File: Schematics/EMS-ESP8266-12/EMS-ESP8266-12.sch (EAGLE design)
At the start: 45 parts, among them IC1 LM393N, J99 Upload, T1 BC547B, T2 BC547B

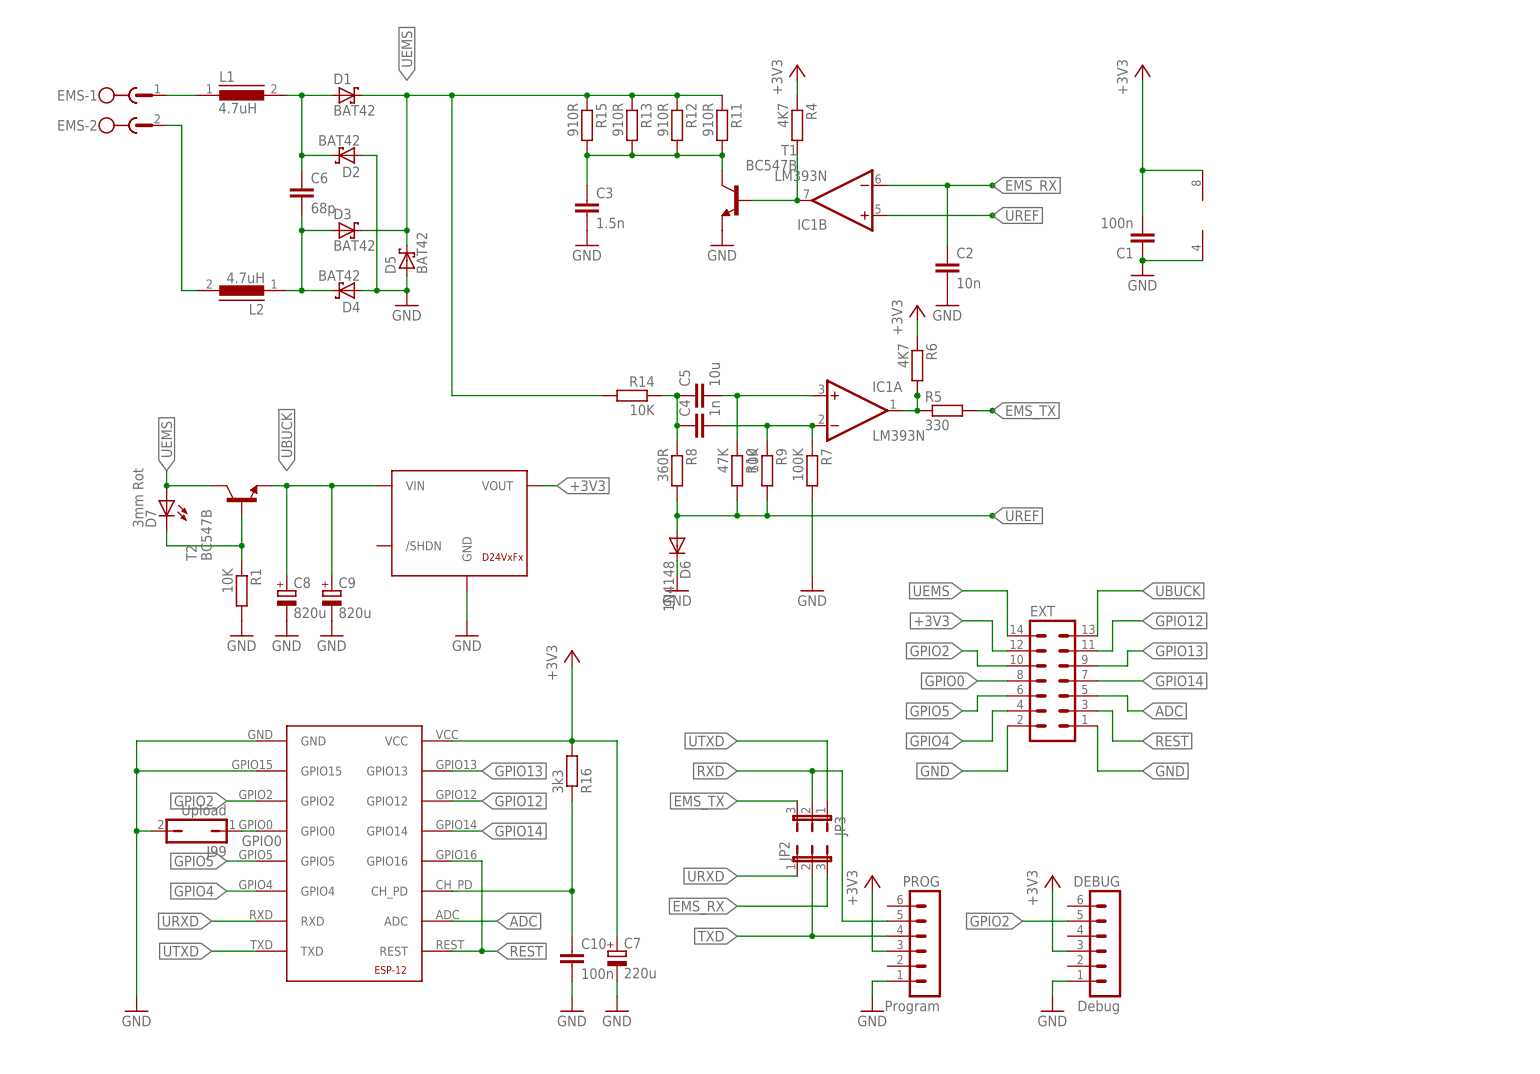
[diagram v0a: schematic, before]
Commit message: PCB reworked ° remove ground layer below ESP12-antenna ° change connector footprint ° 2pin debug connector ° small form factor for EMS connector
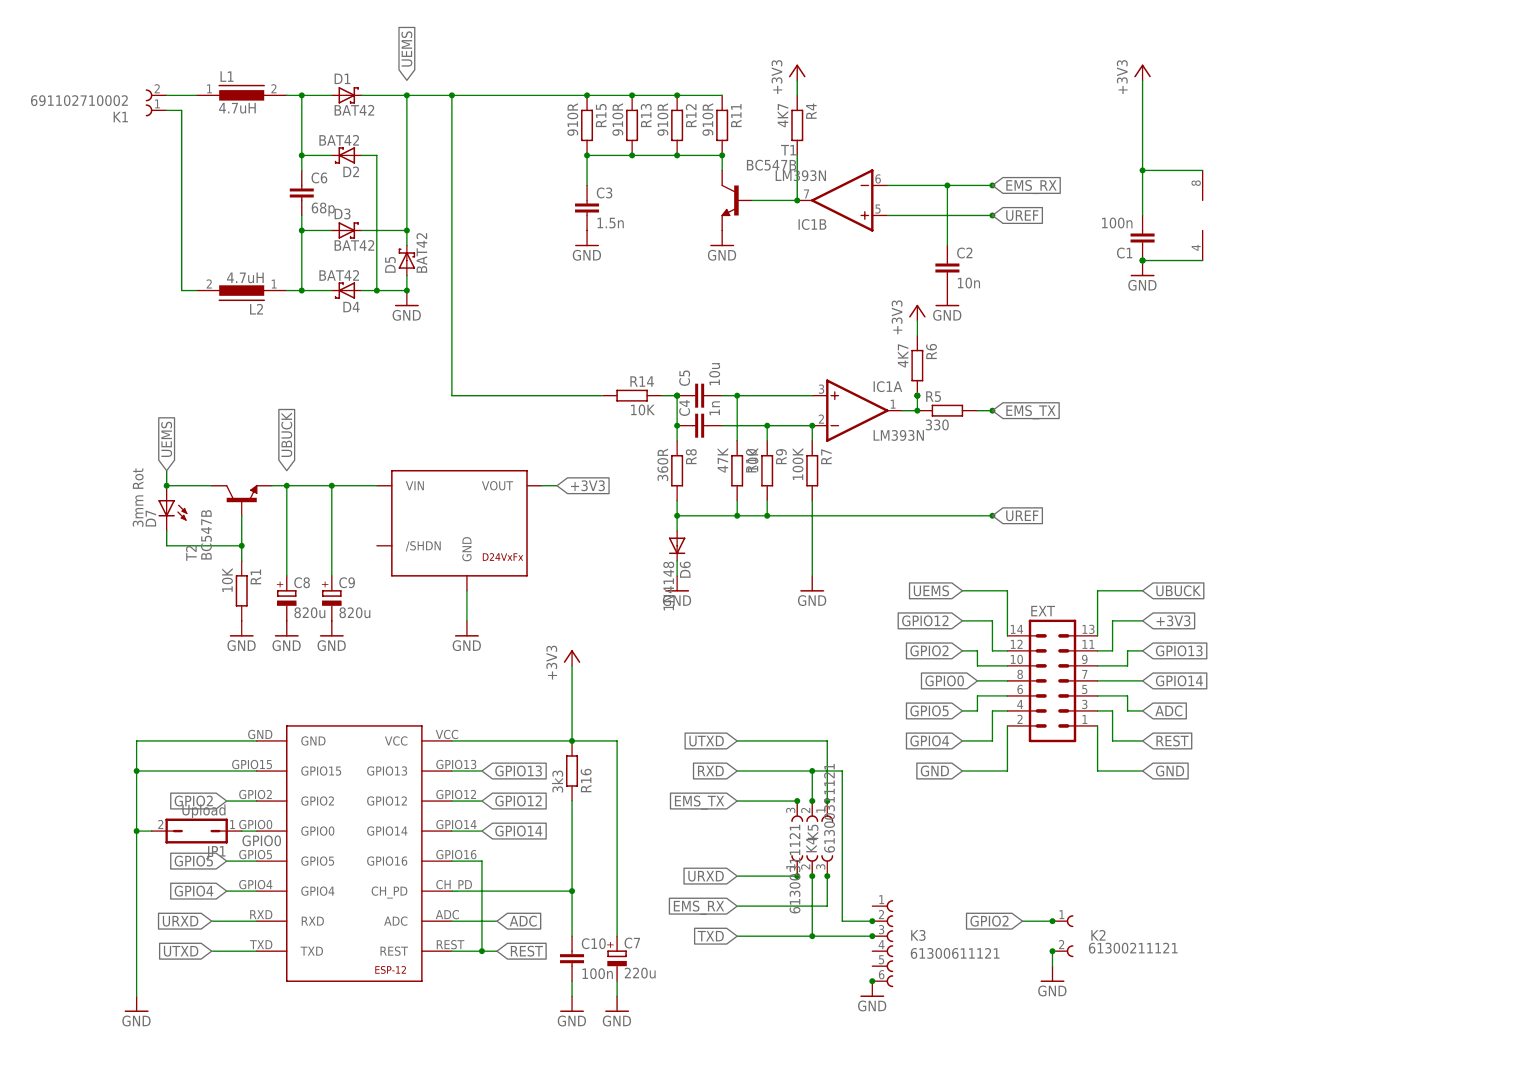
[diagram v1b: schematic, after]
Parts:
- removed DEBUG: Debug, con-lstb:MA06-1
- removed EMS: MST2V, con-phoenix-508:MST2V
- removed JP2, JP3: (no value), jumper:JP2E
- removed PROG: Program, con-lstb:MA06-1
- added K1: 691102710002, EagleLibrary_Wuerth_Elektronik_eiCan_Terminal_Blocks_Connectors_v6_20150113:691102710002
- added K2: 61300211121, EagleLibrary_Wuerth_Elektronik_eiCan_Board_to_Board_Connectors_v6_20150113:61300211121
- added K3: 61300611121, EagleLibrary_Wuerth_Elektronik_eiCan_Board_to_Board_Connectors_v6_20150113:61300611121
- added K4, K5: 61300311121, EagleLibrary_Wuerth_Elektronik_eiCan_Board_to_Board_Connectors_v6_20150113:61300311121
- renumbered J99 to JP1
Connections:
- net +3V3: now also EXT.11; no longer DEBUG.3, EXT.12, PROG.3
- net EMS_RX: now also K4.3; no longer JP2.3
- net EMS_TX: now also K5.3; no longer JP3.3
- net GND: now also K2.2, K3.6; no longer DEBUG.1, PROG.1
- net GPIO12: now also EXT.12; no longer EXT.11
- net GPIO2: now also K2.1; no longer DEBUG.5
- net N$4: now also K1.2; no longer EMS-1.1
- net N$8: now also K1.1; no longer EMS-2.1
- net RXD: now also K3.2, K5.2; no longer JP3.2, PROG.5
- net TXD: now also K3.3, K4.2; no longer JP2.2, PROG.4
- net URXD: now also K4.1; no longer JP2.1
- net UTXD: now also K5.1; no longer JP3.1

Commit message: Redesign - Board Rev. 1.0 - Debug Tx Anschluß entfällt, da bereits auf Ext. Port (GPIO2) - CH_PD auf Ext. Port geführt - Längsregler mit LED anstelle 3er Dioden. Als Seiteneffekt gibts eine   Betriebsanzeige - Farbe ganz nach Gusto... - EMS-Tx Ausgang (LM334) auf 100R reduziert - 4x 910R in 2x 470R optimiert - Bestückung kompakter - Boardgröße 77x50 mm² - RC-Kombination CH_PD und REST lt. Espressif HW-SDK
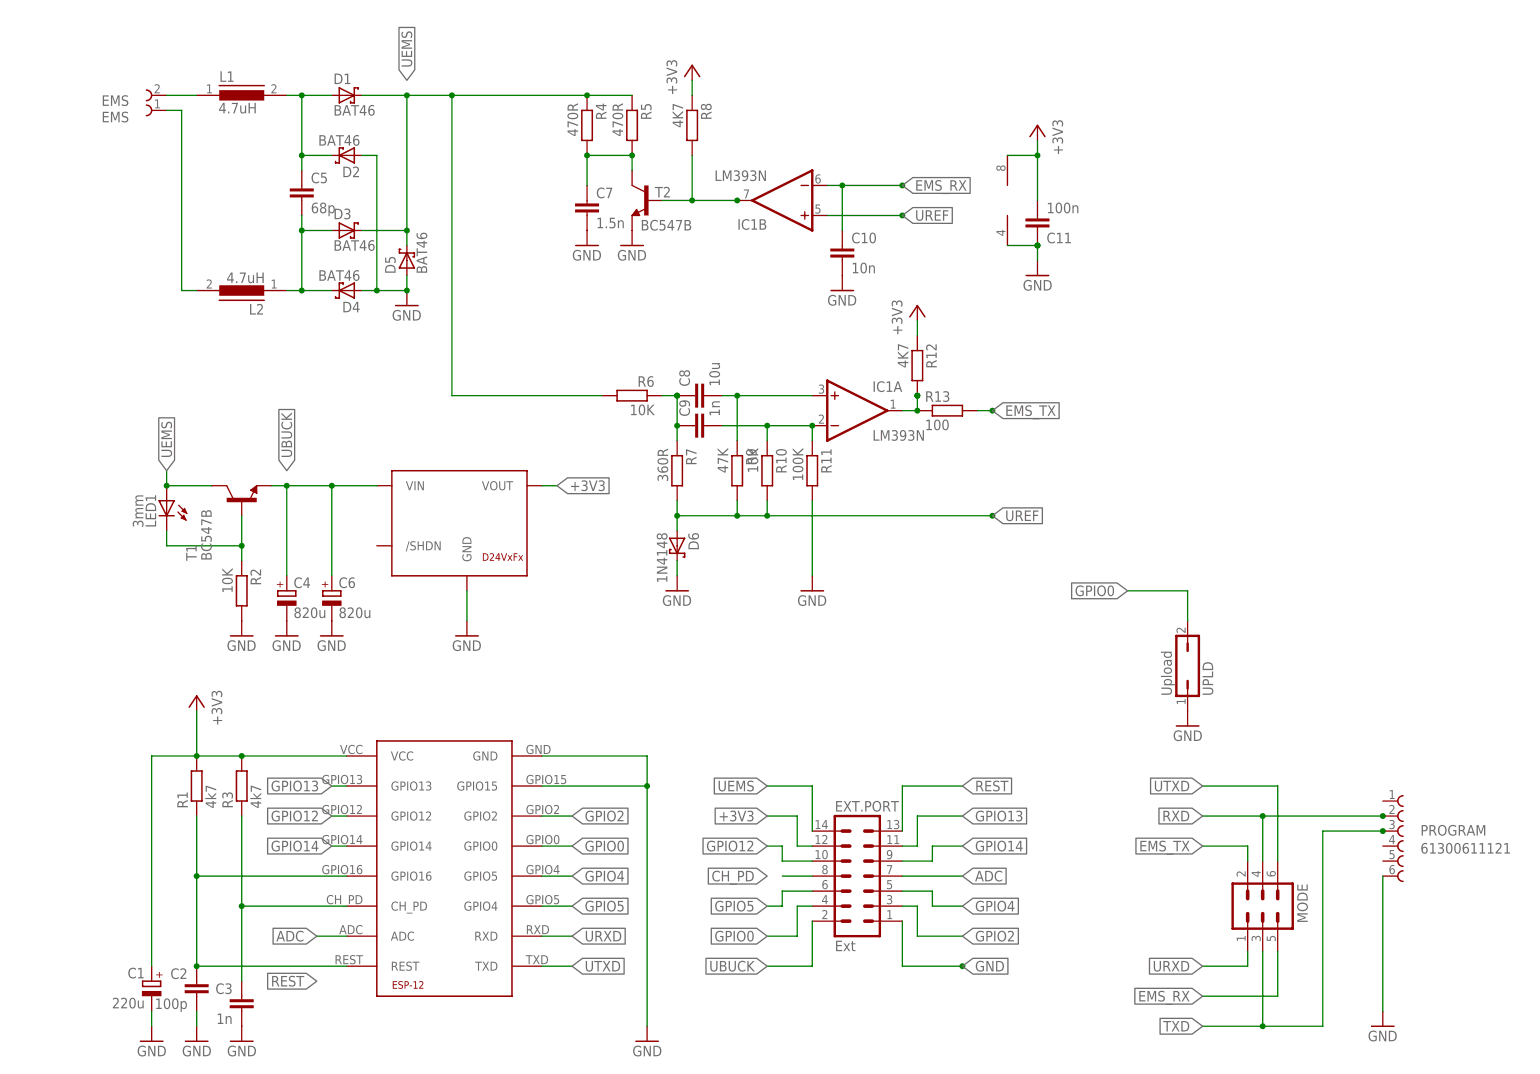
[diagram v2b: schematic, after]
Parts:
- removed EXT: (no value), con-lstb:MA07-2
- removed JP1: Upload, jumper:JP1Q
- removed K2: 61300211121, EagleLibrary_Wuerth_Elektronik_eiCan_Board_to_Board_Connectors_v6_20150113:61300211121
- removed K3: 61300611121, EagleLibrary_Wuerth_Elektronik_eiCan_Board_to_Board_Connectors_v6_20150113:61300611121
- removed K4, K5: 61300311121, EagleLibrary_Wuerth_Elektronik_eiCan_Board_to_Board_Connectors_v6_20150113:61300311121
- removed R14: 10K, resistor:R-EU_0207/10
- removed R15: 910R, resistor:R-EU_0207/10
- removed R16: 3k3, resistor:R-EU_0207/10
- removed U$2: ESP-12ESP-12, ESP8266-ESP12:ESP-12ESP-12
- added C11: 100n, capacitor-wima:C2.5/2
- added ESP1: ESP-12ESP-12, ESP8266-ESP12:ESP-12ESP-12
- added EXT.PORT: Ext, con-lstb:MA07-2
- added MODE: (no value), con-lstb:MA03-2
- added PROGRAM: 61300611121, EagleLibrary_Wuerth_Elektronik_eiCan_Board_to_Board_Connectors_v6_20150113:61300611121
- added R2: 10K, resistor:R-EU_0204/7
- added R3: 4k7, resistor:R-EU_0204/7
- added UPLD: Upload, jumper:JP1Q
- C1: value 100n -> 220u; device capacitor-wima:C2.5/2 -> rcl:CPOL-EUUD-6,3X8,8; CONRAD (none) -> VF 220/6,3 P-D
- C10: value 100n -> 10n
- C2: value 10n -> 100p
- C3: value 1.5n -> 1n
- C4: value 1n -> 820u; device capacitor-wima:C2.5/2 -> rcl:CPOL-EUUD-10X10; CONRAD (none) -> VF 820/16 P-G
- C5: value 10u -> 68p; device capacitor-wima:C5/7.2 -> resistor:C-EU025-050X050; CONRAD (none) -> 457221-62
- C6: value 68p -> 820u; device resistor:C-EU025-050X050 -> rcl:CPOL-EUUD-10X10; CONRAD (none) -> VF 820/16 P-G
- C7: value 220u -> 1.5n; device rcl:CPOL-EUUD-6,3X8,8 -> capacitor-wima:C2.5/2; CONRAD VF 220/6,3 P-D -> (none)
- C8: value 820u -> 10u; device rcl:CPOL-EUUD-10X10 -> capacitor-wima:C5/11; CONRAD VF 820/16 P-G -> 450662-62
- C9: value 820u -> 1n; device rcl:CPOL-EUUD-10X10 -> capacitor-wima:C2.5/2; CONRAD VF 820/16 P-G -> 453005-62
- D1, D2, D3, D4, D5: value BAT42 -> BAT46; device diode:BAT42 -> diode:SCHOTTKY-DIODEDO35-7; CONRAD (none) -> 153087-62
- D6: device diode:1N4148DO35-10 -> diode:SCHOTTKY-DIODEDO35-7; CONRAD (none) -> 162280-62
- EMS: value 691102710002 -> EMS
- L1, L2: CONRAD (none) -> 440391-62
- LED1: value 3mm Rot -> 3mm
- R1: value 10K -> 4k7; device resistor:R-EU_0207/10 -> resistor:R-EU_0204/7
- R10: value 47K -> 10K; device resistor:R-EU_0207/10 -> resistor:R-EU_0204/7
- R11: value 910R -> 100K; device resistor:R-EU_0207/10 -> resistor:R-EU_0204/7
- R12: value 910R -> 4K7; device resistor:R-EU_0207/10 -> resistor:R-EU_0204/7
- R13: value 910R -> 100; device resistor:R-EU_0207/10 -> resistor:R-EU_0204/7
- R4: value 4K7 -> 470R; device resistor:R-EU_0207/10 -> resistor:R-EU_0204/7
- R5: value 330 -> 470R; device resistor:R-EU_0207/10 -> resistor:R-EU_0204/7
- R6: value 4K7 -> 10K; device resistor:R-EU_0207/10 -> resistor:R-EU_0204/7
- R7: value 100K -> 360R; device resistor:R-EU_0207/10 -> resistor:R-EU_0204/7
- R8: value 360R -> 4K7; device resistor:R-EU_0207/10 -> resistor:R-EU_0204/7
- R9: value 10K -> 47K; device resistor:R-EU_0207/10 -> resistor:R-EU_0204/7
- renumbered D7 to LED1, K1 to EMS, U$1 to MOD1
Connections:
- removed net N$3: C10.1, R16.1, U$2.CH_PD
- new net CH_PD: C3.1, ESP1.CH_PD, EXT.PORT.8, R3.1
- new net GPIO15: ESP1.GND, ESP1.GPIO15
- net +3V3: now also C1.+, C11.2, ESP1.VCC, EXT.PORT.12, R1.2, R12.1, R3.2, R8.1; no longer C1.2, C7.+, EXT.11, R16.2, R4.1, R6.1, U$2.VCC
- net ADC: now also ESP1.ADC, EXT.PORT.7; no longer EXT.5, U$2.ADC
- net EMS_RX: now also C10.1, MODE.5; no longer C2.1, K4.3
- net EMS_TX: now also MODE.2, R13.2; no longer K5.3, R5.2
- net GND: now also C1.-, C11.1, C4.-, C6.-, C7.2, EXT.PORT.1, PROGRAM.6, R11.2, R2.2, T2.E, UPLD.1; no longer C1.1, C7.-, C8.-, C9.-, EXT.1, EXT.2, JP1.2, K2.2, K3.6, R1.2, R7.2, T1.E, U$2.GND, U$2.GPIO15
- net GPIO0: now also ESP1.GPIO0, EXT.PORT.4, UPLD.2; no longer EXT.8, JP1.1, U$2.GPIO0
- net GPIO12: now also ESP1.GPIO12, EXT.PORT.10; no longer EXT.12, U$2.GPIO12
- net GPIO13: now also ESP1.GPIO13, EXT.PORT.11; no longer EXT.9, U$2.GPIO13
- net GPIO14: now also ESP1.GPIO14, EXT.PORT.9; no longer EXT.7, U$2.GPIO14
- net GPIO2: now also ESP1.GPIO2, EXT.PORT.3; no longer EXT.10, K2.1, U$2.GPIO2
- net GPIO4: now also ESP1.GPIO5, EXT.PORT.5; no longer EXT.4, U$2.GPIO4
- net GPIO5: now also ESP1.GPIO4, EXT.PORT.6; no longer EXT.6, U$2.GPIO5
- net N$1: now also C5.1; no longer C6.1
- net N$12: now also C9.2, R10.1, R11.1; no longer C4.2, R7.1, R9.1
- net N$15: now also R8.2, T2.B; no longer R4.2, T1.B
- net N$17: now also R2.1, T1.B; no longer R1.1, T2.B
- net N$2: now also C5.2; no longer C6.2
- net N$5: now also R12.2, R13.1; no longer R5.1, R6.2
- net N$6: now also C7.1, R4.2, R5.2, T2.C; no longer C3.1, R11.2, R12.2, R13.2, R15.2, T1.C
- net N$7: now also C8.1, C9.1, R6.1, R7.1; no longer C4.1, C5.1, R14.1, R8.1
- net N$9: now also C8.2, R9.1; no longer C5.2, R10.1
- net REST: now also C2.1, ESP1.GPIO16, ESP1.REST, EXT.PORT.13, R1.1; no longer EXT.3, U$2.GPIO16, U$2.REST
- net RXD: now also MODE.4, PROGRAM.2; no longer K3.2, K5.2
- net TXD: now also MODE.3, PROGRAM.3; no longer K3.3, K4.2
- net UBUCK: now also C4.+, C6.+, EXT.PORT.2, T1.E; no longer C8.+, C9.+, EXT.13, T2.E
- net UEMS: now also EXT.PORT.14, R4.1, R5.1, R6.2, T1.C; no longer EXT.14, R11.1, R12.1, R13.1, R14.2, R15.1, T2.C
- net UREF: now also R7.2; no longer R8.2
- net URXD: now also ESP1.RXD, MODE.1; no longer K4.1, U$2.RXD
- net UTXD: now also ESP1.TXD, MODE.6; no longer K5.1, U$2.TXD
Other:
- moved on the sheet: C10, C2, C3, C5, IC1B, R1, R10, R11, R12, R13, R4, R5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
